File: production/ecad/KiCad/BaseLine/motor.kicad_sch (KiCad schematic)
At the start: 9 parts, among them J1 VibeMotorConnector, U1 DRV8830DGQR

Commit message: Sean DR updates
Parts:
- added C29: 10u, symbol Device:C
- added J8: VibeMotorConnector_2, symbol Connector:Conn_01x02_Socket
- added R28: 0.308, symbol Device:R_US
- added R29, R49, R50: DNP, symbol Device:R_US
- added R51: 0, symbol Device:R_US
- added R52, R53, R54: R_US, symbol Device:R_US
- added TP24: TestPoint_Motor_2, symbol Connector:TestPoint_2Pole
- added U10: DRV8830DGQR, DRV8830DGQR:IC_XTR111AIDGQR, symbol DRV8830DGQR:DRV8830DGQR
- J1: value VibeMotorConnector -> VibeMotorConnector_1
- R1, R3: value 0 -> DNP
- TP23: value TestPoint_Motor -> TestPoint_Motor_1
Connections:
- net +5V: now also C29.1, R29.1, R50.1, U10.4 (VCC)
- net GND: now also C29.2, R28.2, R49.1, R51.1, U10.5 (GND)
- net SCL: now also U10.10 (SCL)
- net SDA: now also U10.9 (SDA)
- net A0_Vibe renamed A0_Vibe_1
- net A1_Vibe renamed A1_Vibe_1
- net FAULTn: no longer names the net of U1.6 (FAULTN)
- net FAULTn: now also R53.1
- new net: J8.2 (Pin_2), TP24.2, U10.1 (OUT2)
- new net: R28.1, U10.2 (ISENSE)
- new net: J8.1 (Pin_1), TP24.1, U10.3 (OUT1)
- new net: R54.1, U10.6 (FAULTN)
- new net +3.3V: R54.2
- new net A0_Vibe_2: R29.2, R49.2, U10.7 (A0)
- new net A1_Vibe_2: R50.2, R51.2, U10.8 (A1)
- new net FAULTn_1: R53.2
- no-connect marks 1 -> 2
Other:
- moved on the sheet: C1, J1, R3, R4, R5, TP23, U1

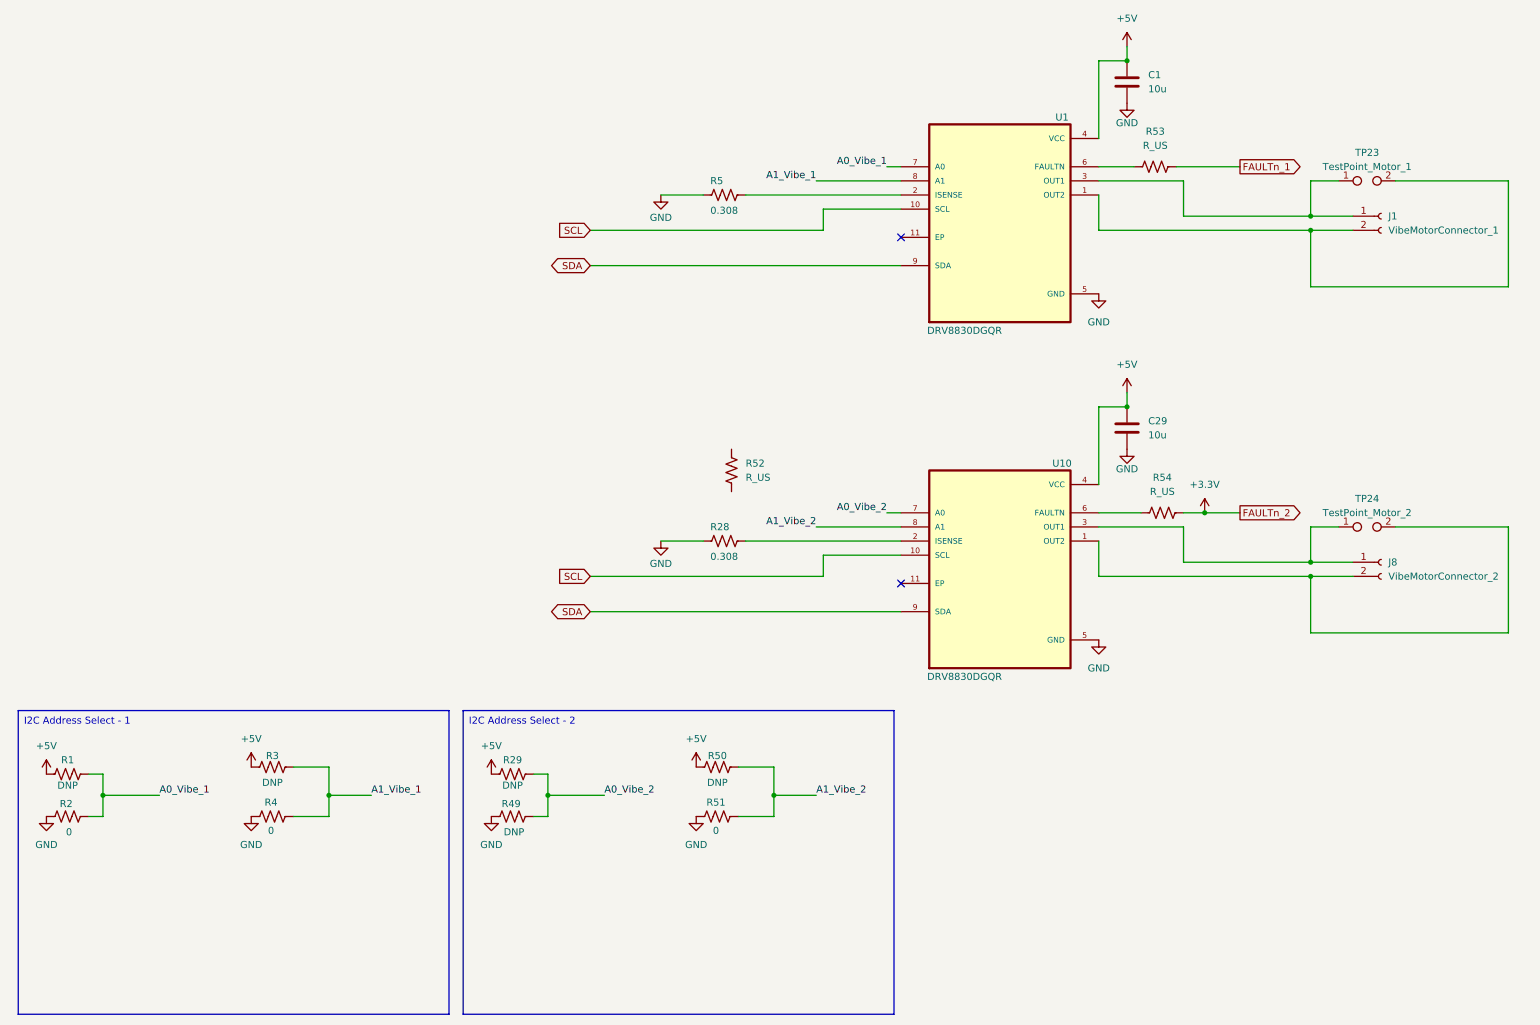
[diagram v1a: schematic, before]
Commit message: Added mux to mcu and fix-ups
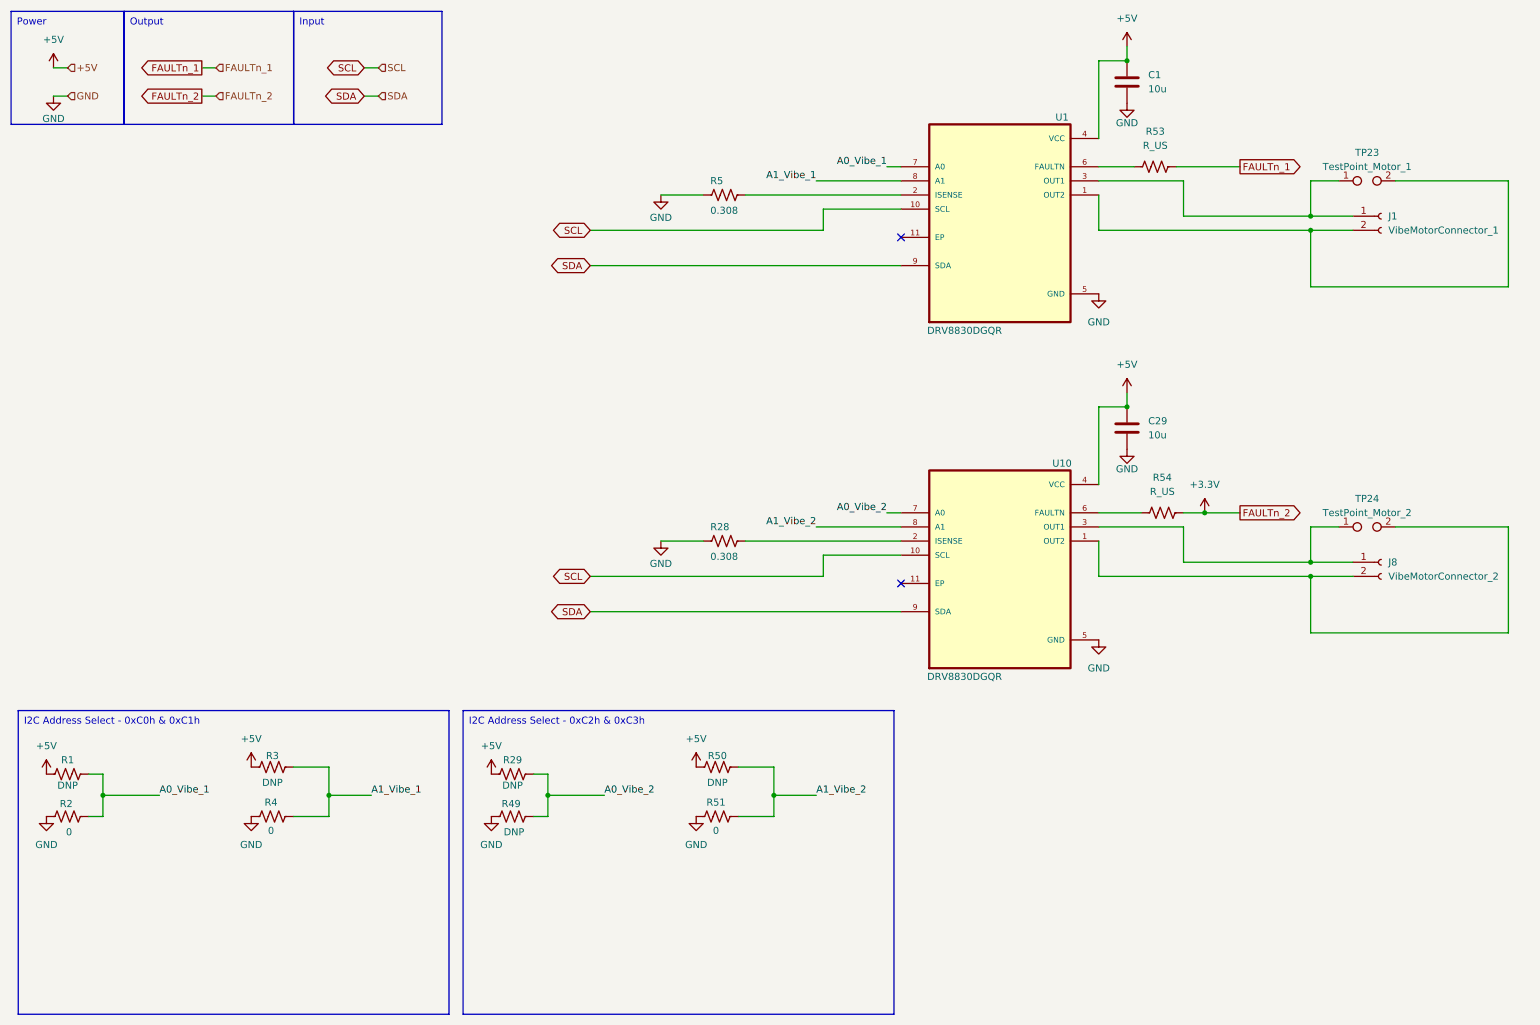
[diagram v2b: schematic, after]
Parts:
- removed R52: R_US, symbol Device:R_US

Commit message: Updated motor schematic
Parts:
- R53, R54: value R_US -> 10k
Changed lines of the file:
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@@
 			)
 		)
-		(property "Value" "R_US"
+		(property "Value" "10k"
 			(at 219.71 101.6 90)
 			(effects
@@
 			)
 		)
-		(property "Value" "R_US"
+		(property "Value" "10k"
 			(at 218.44 39.37 90)
 			(effects

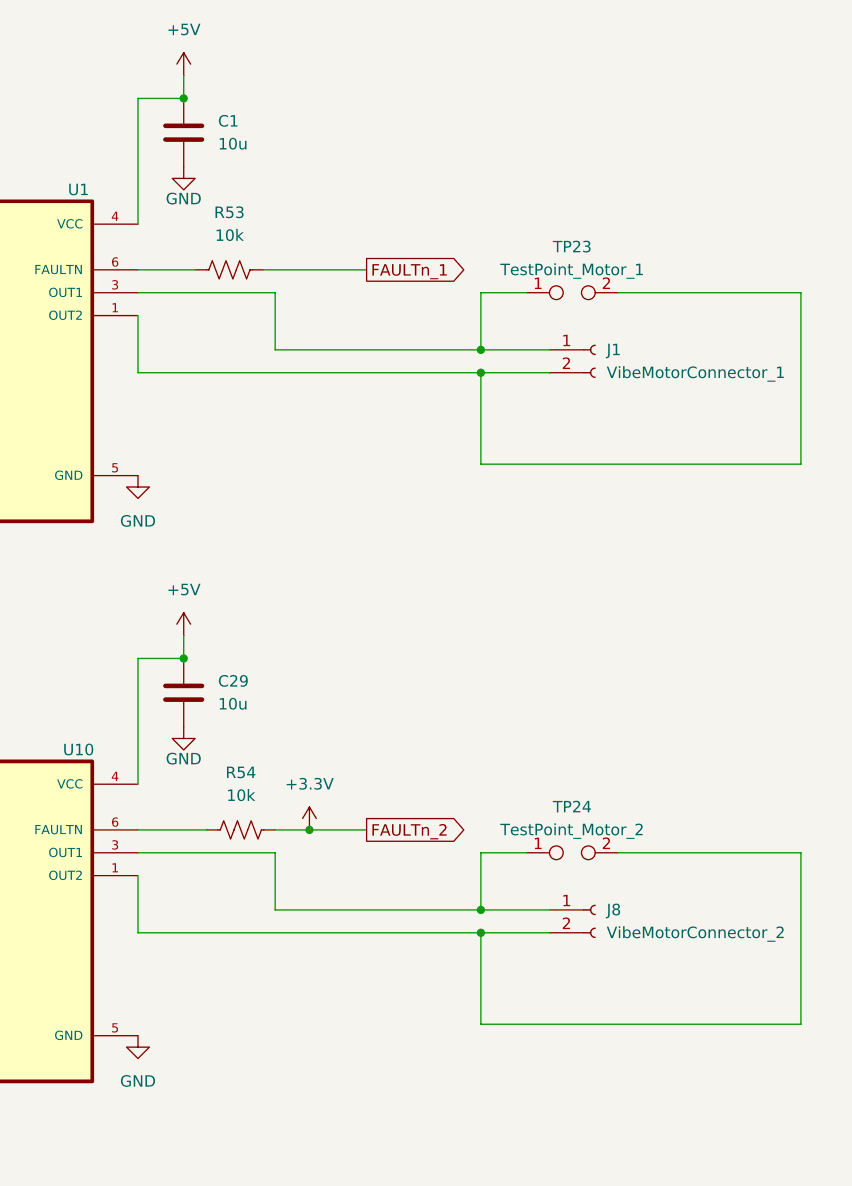
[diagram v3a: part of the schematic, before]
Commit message: Added footprints
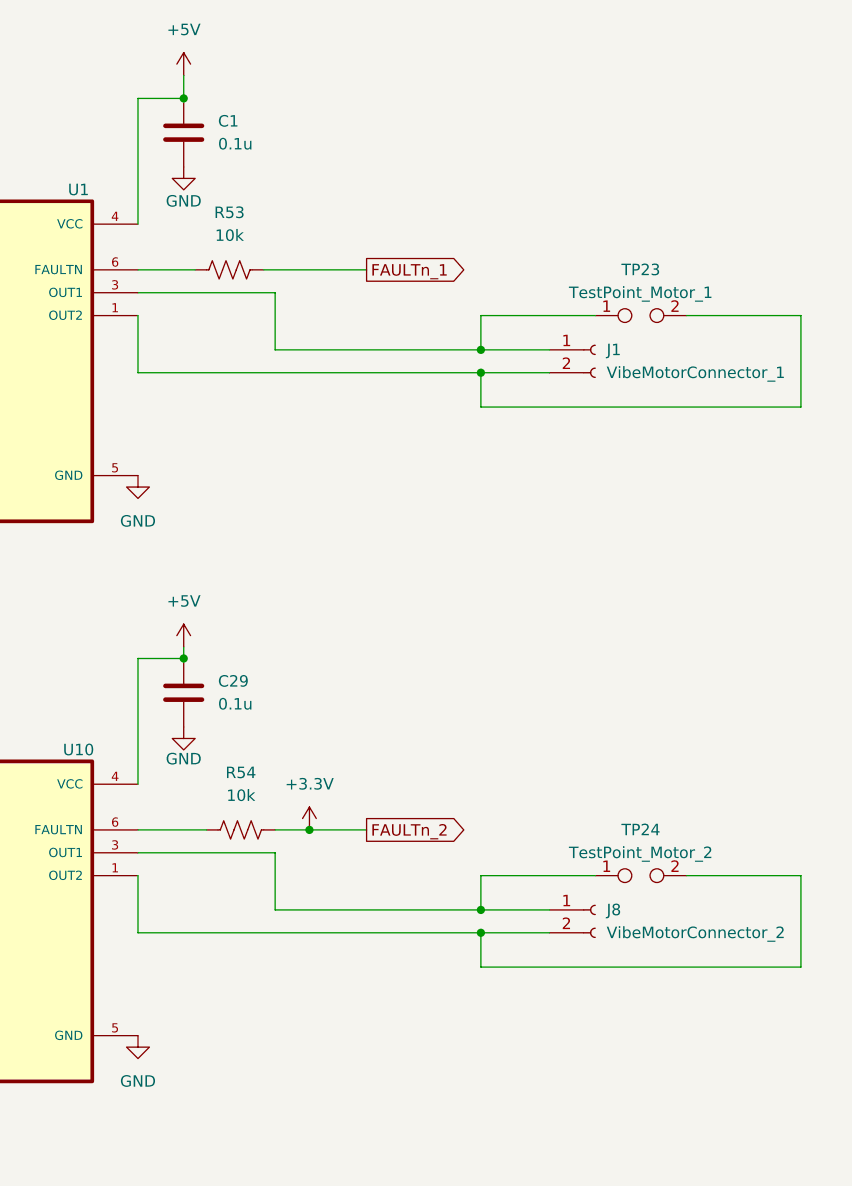
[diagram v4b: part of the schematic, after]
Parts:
- C1, C29: value 10u -> 0.1u; footprint (none) -> Capacitor_SMD:C_0805_2012Metric_Pad1.18x1.45mm_HandSolder
- J1, J8: footprint (none) -> BLT:JST_B2B-XH-A
- R1, R2, R28, R29, R3, R4, R49, R5, R50, R51, R53, R54: footprint (none) -> Resistor_SMD:R_0805_2012Metric_Pad1.20x1.40mm_HandSolder
- TP23, TP24: footprint (none) -> TestPoint:TestPoint_2Pads_Pitch2.54mm_Drill0.8mm
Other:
- moved on the sheet: TP23, TP24
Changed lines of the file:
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@@
 	(wire
 		(pts
-			(xy 213.36 83.82) (xy 213.36 86.36)
+			(xy 213.36 85.09) (xy 213.36 86.36)
 		)
 		(stroke
@@
 	(wire
 		(pts
-			(xy 246.38 107.95) (xy 246.38 114.3)
+			(xy 246.38 110.49) (xy 246.38 114.3)
 		)
 		(stroke
@@
 	(wire
 		(pts
-			(xy 281.94 127) (xy 281.94 107.95)
+			(xy 281.94 120.65) (xy 281.94 110.49)
 		)
 		(stroke
@@
 	(wire
 		(pts
-			(xy 246.38 54.61) (xy 246.38 64.77)
+			(xy 246.38 54.61) (xy 246.38 58.42)
 		)
 		(stroke
@@
 	(wire
 		(pts
-			(xy 246.38 116.84) (xy 246.38 127)
+			(xy 246.38 116.84) (xy 246.38 120.65)
 		)
 		(stroke
@@
 	(wire
 		(pts
-			(xy 246.38 45.72) (xy 246.38 52.07)
+			(xy 246.38 48.26) (xy 246.38 52.07)
 		)
 		(stroke
@@
 	(wire
 		(pts
-			(xy 281.94 107.95) (xy 261.62 107.95)
+			(xy 281.94 110.49) (xy 269.24 110.49)
 		)
 		(stroke
@@
 	(wire
 		(pts
-			(xy 246.38 127) (xy 281.94 127)
+			(xy 246.38 120.65) (xy 281.94 120.65)
 		)
 		(stroke
@@
 	(wire
 		(pts
-			(xy 251.46 45.72) (xy 246.38 45.72)
+			(xy 259.08 48.26) (xy 246.38 48.26)
 		)
 		(stroke
@@
 	(wire
 		(pts
-			(xy 281.94 64.77) (xy 281.94 45.72)
+			(xy 281.94 58.42) (xy 281.94 48.26)
 		)
 		(stroke
@@
 	(wire
 		(pts
-			(xy 281.94 45.72) (xy 261.62 45.72)
+			(xy 281.94 48.26) (xy 269.24 48.26)
 		)
 		(stroke
@@
 	(wire
 		(pts
-			(xy 246.38 64.77) (xy 281.94 64.77)
+			(xy 246.38 58.42) (xy 281.94 58.42)
 		)
 		(stroke
@@
 	(wire
 		(pts
-			(xy 251.46 107.95) (xy 246.38 107.95)
+			(xy 259.08 110.49) (xy 246.38 110.49)
 		)
 		(stroke
@@
 	)
 	(image
-		(at 92.71 -27.94)
+		(at 46.99 54.61)
 		(scale 0.222671)
 		(data "iVBORw0KGgoAAAANSUhEUgAAA2kAAAKPCAYAAAD34oKNAAAAAXNSR0IArs4c6QAAAARnQU1BAACx"
@@
 	(symbol
 		(lib_id "Connector:TestPoint_2Pole")
-		(at 256.54 45.72 0)
+		(at 264.16 48.26 0)
 		(unit 1)
 		(exclude_from_sim no)
@@
 		(fields_autoplaced yes)
 		(property "Reference" "TP23"
-			(at 256.54 40.64 0)
+			(at 264.16 43.18 0)
 			(effects
 				(font
@@
 		)
 		(property "Value" "TestPoint_Motor_1"
-			(at 256.54 43.18 0)
+			(at 264.16 45.72 0)
 			(effects
 				(font
@@
 			)
 		)
-		(property "Footprint" ""
-			(at 256.54 45.72 0)
+		(property "Footprint" "TestPoint:TestPoint_2Pads_Pitch2.54mm_Drill0.8mm"
+			(at 264.16 48.26 0)
 			(effects
 				(font
@@
 		)
 		(property "Datasheet" "~"
-			(at 256.54 45.72 0)
+			(at 264.16 48.26 0)
 			(effects
 				(font
@@
 		)
 		(property "Description" "2-polar test point"
-			(at 256.54 45.72 0)
+			(at 264.16 48.26 0)
 			(effects
 				(font
@@
 			)
 		)
-		(property "Footprint" ""
+		(property "Footprint" "Resistor_SMD:R_0805_2012Metric_Pad1.20x1.40mm_HandSolder"
 			(at 23.114 159.004 90)
 			(effects
@@
 	(symbol
 		(lib_id "power:+5V")
-		(at 213.36 83.82 0)
+		(at 213.36 85.09 0)
 		(unit 1)
 		(exclude_from_sim no)
@@
 		(fields_autoplaced yes)
 		(property "Reference" "#PWR083"
-			(at 213.36 87.63 0)
+			(at 213.36 88.9 0)
 			(effects
 				(font
@@
 		)
 		(property "Value" "+5V"
-			(at 213.36 78.74 0)
+			(at 213.36 80.01 0)
 			(effects
 				(font
@@
 		)
 		(property "Footprint" ""
-			(at 213.36 83.82 0)
+			(at 213.36 85.09 0)
 			(effects
 				(font
@@
 		)
 		(property "Datasheet" ""
-			(at 213.36 83.82 0)
+			(at 213.36 85.09 0)
 			(effects
 				(font
@@
 		)
 		(property "Description" "Power symbol creates a global label with name \"+5V\""
-			(at 213.36 83.82 0)
+			(at 213.36 85.09 0)
 			(effects
 				(font
@@
 			)
 		)
-		(property "Footprint" ""
+		(property "Footprint" "Resistor_SMD:R_0805_2012Metric_Pad1.20x1.40mm_HandSolder"
 			(at 139.954 150.114 90)
 			(effects
@@
 			)
 		)
-		(property "Footprint" ""
+		(property "Footprint" "Resistor_SMD:R_0805_2012Metric_Pad1.20x1.40mm_HandSolder"
 			(at 139.954 159.004 90)
 			(effects
@@
 			)
 		)
-		(property "Footprint" ""
+		(property "Footprint" "Resistor_SMD:R_0805_2012Metric_Pad1.20x1.40mm_HandSolder"
 			(at 103.124 159.004 90)
 			(effects
@@
 			)
 		)
-		(property "Footprint" ""
+		(property "Footprint" "Resistor_SMD:R_0805_2012Metric_Pad1.20x1.40mm_HandSolder"
 			(at 140.716 49.276 90)
 			(effects
@@
 	(symbol
 		(lib_id "Connector:TestPoint_2Pole")
-		(at 256.54 107.95 0)
+		(at 264.16 110.49 0)
 		(unit 1)
 		(exclude_from_sim no)
@@
 		(fields_autoplaced yes)
 		(property "Reference" "TP24"
-			(at 256.54 102.87 0)
+			(at 264.16 105.41 0)
 			(effects
 				(font
@@
 		)
 		(property "Value" "TestPoint_Motor_2"
-			(at 256.54 105.41 0)
+			(at 264.16 107.95 0)
 			(effects
 				(font
@@
 			)
 		)
-		(property "Footprint" ""
-			(at 256.54 107.95 0)
+		(property "Footprint" "TestPoint:TestPoint_2Pads_Pitch2.54mm_Drill0.8mm"
+			(at 264.16 110.49 0)
 			(effects
 				(font
@@
 		)
 		(property "Datasheet" "~"
-			(at 256.54 107.95 0)
+			(at 264.16 110.49 0)
 			(effects
 				(font
@@
 		)
 		(property "Description" "2-polar test point"
-			(at 256.54 107.95 0)
+			(at 264.16 110.49 0)
 			(effects
 				(font
@@
 			)
 		)
-		(property "Footprint" ""
+		(property "Footprint" "Resistor_SMD:R_0805_2012Metric_Pad1.20x1.40mm_HandSolder"
 			(at 140.716 111.506 90)
 			(effects
@@
 			)
 		)
-		(property "Footprint" ""
+		(property "Footprint" "Resistor_SMD:R_0805_2012Metric_Pad1.20x1.40mm_HandSolder"
 			(at 59.944 159.004 90)
 			(effects
@@
 			)
 		)
-		(property "Footprint" ""
+		(property "Footprint" "Resistor_SMD:R_0805_2012Metric_Pad1.20x1.40mm_HandSolder"
 			(at 23.114 151.384 90)
 			(effects
@@
 			)
 		)
-		(property "Value" "10u"
+		(property "Value" "0.1u"
 			(at 217.17 91.4399 0)
 			(effects
@@
 			)
 		)
-		(property "Footprint" ""
+		(property "Footprint" "Capacitor_SMD:C_0805_2012Metric_Pad1.18x1.45mm_HandSolder"
 			(at 214.3252 93.98 0)
 			(effects
@@
 			)
 		)
-		(property "Footprint" ""
+		(property "Footprint" "BLT:JST_B2B-XH-A"
 			(at 259.08 52.07 0)
 			(effects
@@
 			)
 		)
-		(property "Value" "10u"
+		(property "Value" "0.1u"
 			(at 217.17 29.2099 0)
 			(effects
@@
 			)
 		)
-		(property "Footprint" ""
+		(property "Footprint" "Capacitor_SMD:C_0805_2012Metric_Pad1.18x1.45mm_HandSolder"
 			(at 214.3252 31.75 0)
 			(effects
@@
 			)
 		)
-		(property "Footprint" ""
+		(property "Footprint" "Resistor_SMD:R_0805_2012Metric_Pad1.20x1.40mm_HandSolder"
 			(at 219.964 104.394 90)
 			(effects
@@
 		)
 		(property "Value" "GND"
-			(at 213.36 35.306 0)
+			(at 213.36 35.56 0)
 			(effects
 				(font
@@
 			)
 		)
-		(property "Footprint" ""
+		(property "Footprint" "BLT:JST_B2B-XH-A"
 			(at 259.08 114.3 0)
 			(effects
@@
 			)
 		)
-		(property "Footprint" ""
+		(property "Footprint" "Resistor_SMD:R_0805_2012Metric_Pad1.20x1.40mm_HandSolder"
 			(at 218.694 42.164 90)
 			(effects
@@
 			)
 		)
-		(property "Footprint" ""
+		(property "Footprint" "Resistor_SMD:R_0805_2012Metric_Pad1.20x1.40mm_HandSolder"
 			(at 59.944 150.114 90)
 			(effects
@@
 			)
 		)
-		(property "Footprint" ""
+		(property "Footprint" "Resistor_SMD:R_0805_2012Metric_Pad1.20x1.40mm_HandSolder"
 			(at 103.124 151.384 90)
 			(effects
